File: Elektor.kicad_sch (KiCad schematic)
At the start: 54 parts, among them J1 Conn_Coaxial, J13 Conn_Coaxial, J6 Conn_01x03_Pin, J7 Conn_01x02, J8 Conn_01x02, Q1 BF545B, U1 Si5351A-B-GT, U2 74HC74, U3 74HC4066D_653, U5 MCP6022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

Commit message: routage plus compact
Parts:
- removed J7: Conn_01x02, Connector_PinHeader_2.54mm:PinHeader_1x02_P2.54mm_Vertical, symbol Connector_Generic:Conn_01x02
- removed U2: 74HC74, Package_SO:SO-14_5.3x10.2mm_P1.27mm, symbol 74xx:74HC74
- added C14, C8: 4.7u, Capacitor_THT:C_Rect_L4.0mm_W2.5mm_P2.50mm, symbol Device:C_Polarized
- added U2: 74HC04, Package_SO:SOIC-14_3.9x8.7mm_P1.27mm, symbol 74xx:74HC04
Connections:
- net 5VA: now also C15.1
- net GND: now also U2.7 (GND); no longer C15.2
- net GNDA: now also C15.2
- net at C16.1, R5.1, U3.14 (VCC)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: now also U2.11, U2.13, U2.14 (VCC), U2.5, U2.9; no longer C15.1
- net at U1.10 (CLK0): now also U3.5 (2E), U2.1
- net at R17.2, U7.7: now also C14.1; no longer U6.INR
- net at R12.2, U5.7: now also C8.1; no longer U6.INL
- net at U1.9 (CLK1): now also U3.6 (3E), U2.3
- net at U3.12 (4E): now also U2.4
- net at U3.13 (1E): now also U2.2
- new net: C14.2, U6.INR
- new net: C8.2, U6.INL
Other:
- moved on the sheet: C15, C16, C17, C18, R19, R5, U5C, U7C

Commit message: plus compact
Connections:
- net at R1.2, R4.1: now also U6.18 (SDA); no longer U6.19 (SCL)
- net at R2.2, R3.1: now also U6.19 (SCL); no longer U6.18 (SDA)
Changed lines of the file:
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@@
     (stroke (width 0) (type default))
   )
-  (wire (pts (xy 22.86 71.12) (xy 22.86 147.32))
+  (wire (pts (xy 22.86 71.12) (xy 22.86 149.86))
     (stroke (width 0) (type default))
   )
@@
     (stroke (width 0) (type default))
   )
-  (wire (pts (xy 22.86 147.32) (xy 27.94 147.32))
-    (stroke (width 0) (type default))
-  )
   (wire (pts (xy 109.22 40.64) (xy 91.44 40.64))
     (stroke (width 0) (type default))
@@
     (stroke (width 0) (type default))
   )
+  (wire (pts (xy 22.86 149.86) (xy 27.94 149.86))
+    (stroke (width 0) (type default))
+  )
   (wire (pts (xy 85.09 66.04) (xy 88.9 66.04))
     (stroke (width 0) (type default))
@@
     (stroke (width 0) (type default))
   )
+  (wire (pts (xy 24.13 147.32) (xy 27.94 147.32))
+    (stroke (width 0) (type default))
+  )
   (wire (pts (xy 135.89 121.92) (xy 135.89 123.19))
     (stroke (width 0) (type default))
@@
     (stroke (width 0) (type default))
   )
-  (wire (pts (xy 24.13 78.74) (xy 24.13 149.86))
+  (wire (pts (xy 24.13 78.74) (xy 24.13 147.32))
     (stroke (width 0) (type default))
   )
@@
     (stroke (width 0) (type default))
   )
-  (wire (pts (xy 24.13 149.86) (xy 27.94 149.86))
-    (stroke (width 0) (type default))
-  )

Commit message: 4066 avait 16 broches au lieu de 14 !
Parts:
- U3: footprint Package_SO:SO-16_3.9x9.9mm_P1.27mm -> Package_SO:SOIC-14_3.9x8.7mm_P1.27mm
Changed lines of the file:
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@@
       (effects (font (size 1.27 1.27)))
     )
-    (property "Footprint" "Package_SO:SO-16_3.9x9.9mm_P1.27mm" (at 138.43 104.14 0)
+    (property "Footprint" "Package_SO:SOIC-14_3.9x8.7mm_P1.27mm" (at 138.43 104.14 0)
       (effects (font (size 1.27 1.27)) (justify bottom) hide)
     )

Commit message: debut V2
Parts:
- added J10, J2, J3, J4, J5, J7, J9: Conn_01x01_Pin, TestPoint:TestPoint_Loop_D1.80mm_Drill1.0mm_Beaded, symbol Connector:Conn_01x01_Pin
- added R20, R21: 1K, Resistor_SMD:R_0603_1608Metric, symbol Device:R
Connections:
- net at Q1.1 (S), R6.2, R7.2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: now also J7.1 (Pin_1)
- net at C5.1, R13.1, U3.2 (1Z): now also U5.3 (+); no longer U5.2 (-)
- net at U1.10 (CLK0), U2.1, U3.5 (2E): now also J4.1 (Pin_1)
- net at R15.2, U7.1, U7.5 (+): now also J9.1 (Pin_1)
- net at U1.9 (CLK1), U2.3, U3.6 (3E): now also J5.1 (Pin_1)
- net at R14.2, R15.1: now also U7.2 (-); no longer U7.3 (+)
- net at R10.1, R9.2: now also U5.2 (-); no longer U5.3 (+)
- net at R10.2, U5.1, U5.5 (+): now also J10.1 (Pin_1)
- net at C14.2: now also J3.1 (Pin_1), R21.2; no longer U6.INR
- net at C11.1, R18.1, U3.11 (4Y): now also U7.3 (+); no longer U7.2 (-)
- net at U6.INL: now also R20.1; no longer C8.2
- new net: C8.2, J2.1 (Pin_1), R20.2
- new net: R21.1, U6.INR
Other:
- title: (none) -> Elektor SDR for teensy

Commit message: release V1.1
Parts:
- removed J13: Conn_Coaxial, Connector_Coaxial:SMA_Samtec_SMA-J-P-X-ST-EM1_EdgeMount, symbol Connector:Conn_Coaxial
- removed J6: Conn_01x03_Pin, Connector_PinHeader_2.54mm:PinHeader_1x03_P2.54mm_Vertical, symbol Connector:Conn_01x03_Pin
- removed J8: Conn_01x02, Connector_PinHeader_2.54mm:PinHeader_1x02_P2.54mm_Vertical, symbol Connector_Generic:Conn_01x02
- removed RV1: 1K, Potentiometer_THT:Potentiometer_ACP_CA9-H5_Horizontal, symbol Device:R_Potentiometer_Trim
- added R22: 10K, Resistor_SMD:R_0402_1005Metric, symbol Device:R
- added TP_GNDA1, TP_GNDD1: Conn_01x01_Pin, Library_test_point:Test_point_jose_D1.8mm_Drill1.0mm, symbol Connector:Conn_01x01_Pin
- TP2: renamed from J2; footprint TestPoint:TestPoint_Loop_D1.80mm_Drill1.0mm_Beaded -> Library_test_point:Test_point_jose_D1.8mm_Drill1.0mm
- TP3: renamed from J3; footprint TestPoint:TestPoint_Loop_D1.80mm_Drill1.0mm_Beaded -> Library_test_point:Test_point_jose_D1.8mm_Drill1.0mm
- TP4: renamed from J4; footprint TestPoint:TestPoint_Loop_D1.80mm_Drill1.0mm_Beaded -> Library_test_point:Test_point_jose_D1.8mm_Drill1.0mm
- TP5: renamed from J5; footprint TestPoint:TestPoint_Loop_D1.80mm_Drill1.0mm_Beaded -> Library_test_point:Test_point_jose_D1.8mm_Drill1.0mm
- TP6: renamed from J7; footprint TestPoint:TestPoint_Loop_D1.80mm_Drill1.0mm_Beaded -> Library_test_point:Test_point_jose_D1.8mm_Drill1.0mm
- TP7: renamed from J10; footprint TestPoint:TestPoint_Loop_D1.80mm_Drill1.0mm_Beaded -> Library_test_point:Test_point_jose_D1.8mm_Drill1.0mm
- TP8: renamed from J9; footprint TestPoint:TestPoint_Loop_D1.80mm_Drill1.0mm_Beaded -> Library_test_point:Test_point_jose_D1.8mm_Drill1.0mm
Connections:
- net 3.3V: now also R5.1
- net GND: now also TP_GNDD1.1 (Pin_1); no longer R19.1
- net GNDA: now also TP_GNDA1.1 (Pin_1)
- net at C16.1, U2.11, U2.13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: no longer R5.1
- net at Q1.1 (S), R6.2, R7.2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: now also R22.2
- net at Y1.2: now also U1.2 (XA)
- net at U1.6 (CLK2): now also R22.1
- net 5VA renamed 3.3VA
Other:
- moved on the sheet: C15, C17, C18, C19, D1, D2, J1, L1, L2, Q1, R19, R5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

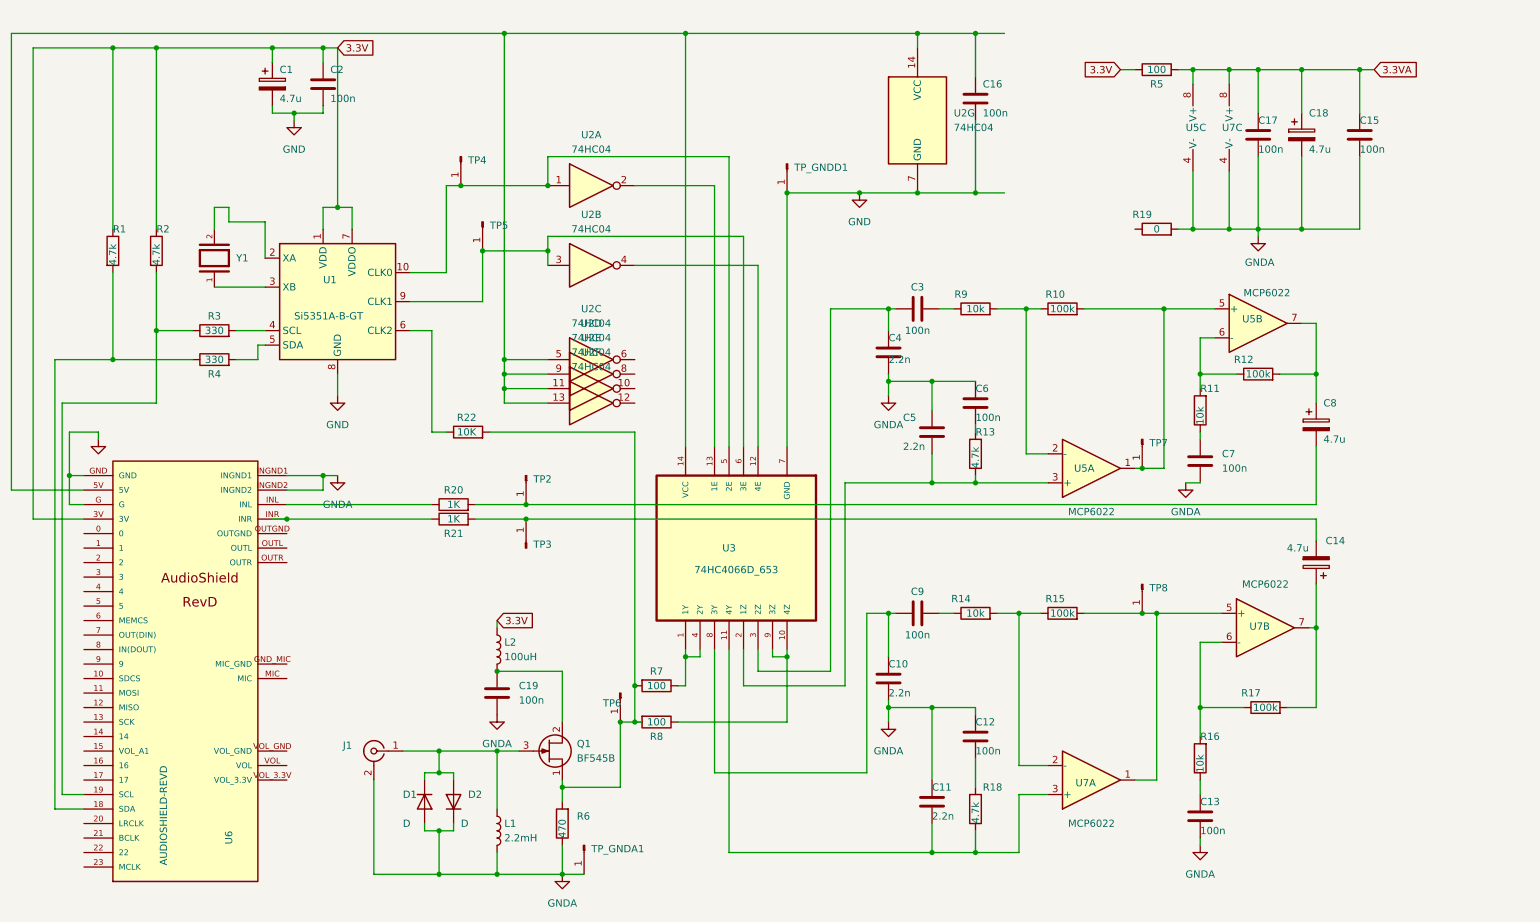
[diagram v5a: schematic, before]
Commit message: version 2.0 using a SN74CBTLV3253
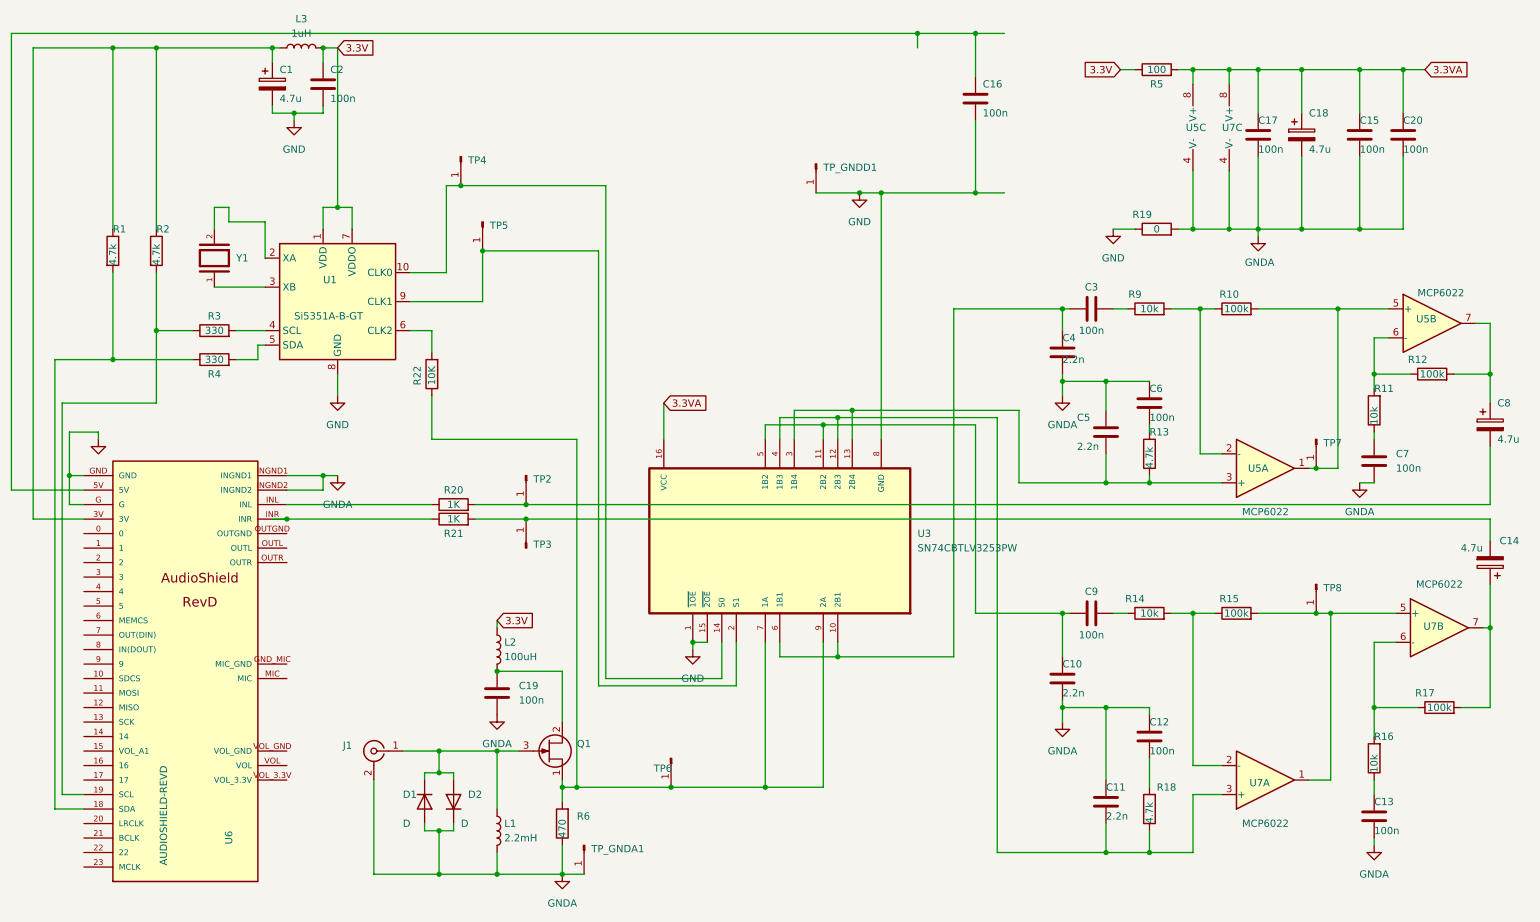
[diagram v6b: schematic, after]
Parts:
- removed R7, R8: 100, Resistor_SMD:R_0603_1608Metric, symbol Device:R
- removed U2: 74HC04, Package_SO:SOIC-14_3.9x8.7mm_P1.27mm, symbol 74xx:74HC04
- removed U3: 74HC4066D_653, Package_SO:SOIC-14_3.9x8.7mm_P1.27mm, symbol 74HC4066D_653:74HC4066D_653
- added C20: 100n, Capacitor_SMD:C_0603_1608Metric, symbol Device:C
- added L3: 1uH, Inductor_SMD:L_0805_2012Metric_Pad1.05x1.20mm_HandSolder, symbol Device:L
- added U3: SN74CBTLV3253PW, Package_SO:TSSOP-16_4.4x5mm_P0.65mm, symbol SN74CBTLV3253PW:SN74CBTLV3253PW
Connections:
- net 3.3V: now also L3.2; no longer C1.1, R1.1, R2.1, U6.3V
- net 3.3VA: now also C20.1, U3.16 (VCC)
- net GND: now also R19.1, U3.1 (~{1OE}), U3.15 (~{2OE}), U3.8 (GND)
- net GNDA: now also C20.2
- net at Q1.1 (S), R6.2, TP6.1 (Pin_1): now also R22.1, U3.7 (1A), U3.9 (2A); no longer R22.2
- net at TP5.1 (Pin_1), U1.9 (CLK1): now also U3.2 (S1)
- net at C5.1, R13.1, U5.3 (+): now also U3.13 (2B4), U3.3 (1B4)
- net at TP4.1 (Pin_1), U1.10 (CLK0): now also U3.14 (S0)
- net at C10.2, C9.1: now also U3.11 (2B2), U3.5 (1B2)
- net at C3.1, C4.2: now also U3.10 (2B1), U3.6 (1B1)
- net at U1.6 (CLK2): now also R22.2; no longer R22.1
- net at C11.1, R18.1, U7.3 (+): now also U3.12 (2B3), U3.4 (1B3)
- new net: C1.1, L3.1, R1.1, R2.1, U6.3V
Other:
- moved on the sheet: C10, C11, C12, C13, C14, C3, C4, C5, C6, C7, C8, C9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
